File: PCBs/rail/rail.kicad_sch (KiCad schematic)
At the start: 3 parts

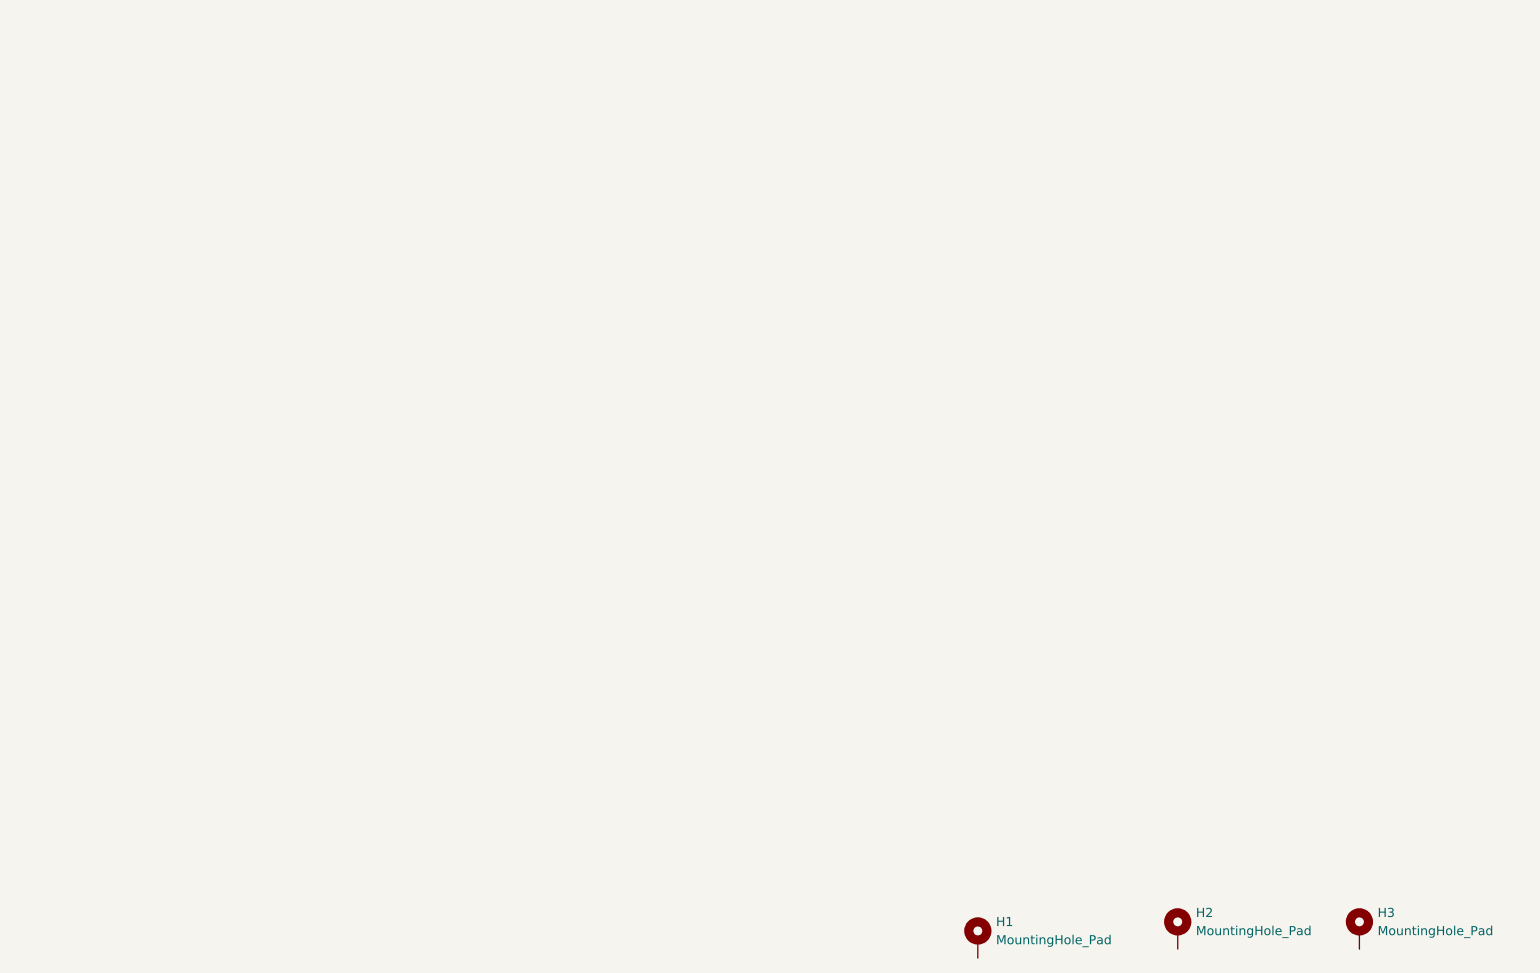
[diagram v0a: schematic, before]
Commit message: Torso, bogie and rail complete. Next up: revise hand and IMU board in conjunction
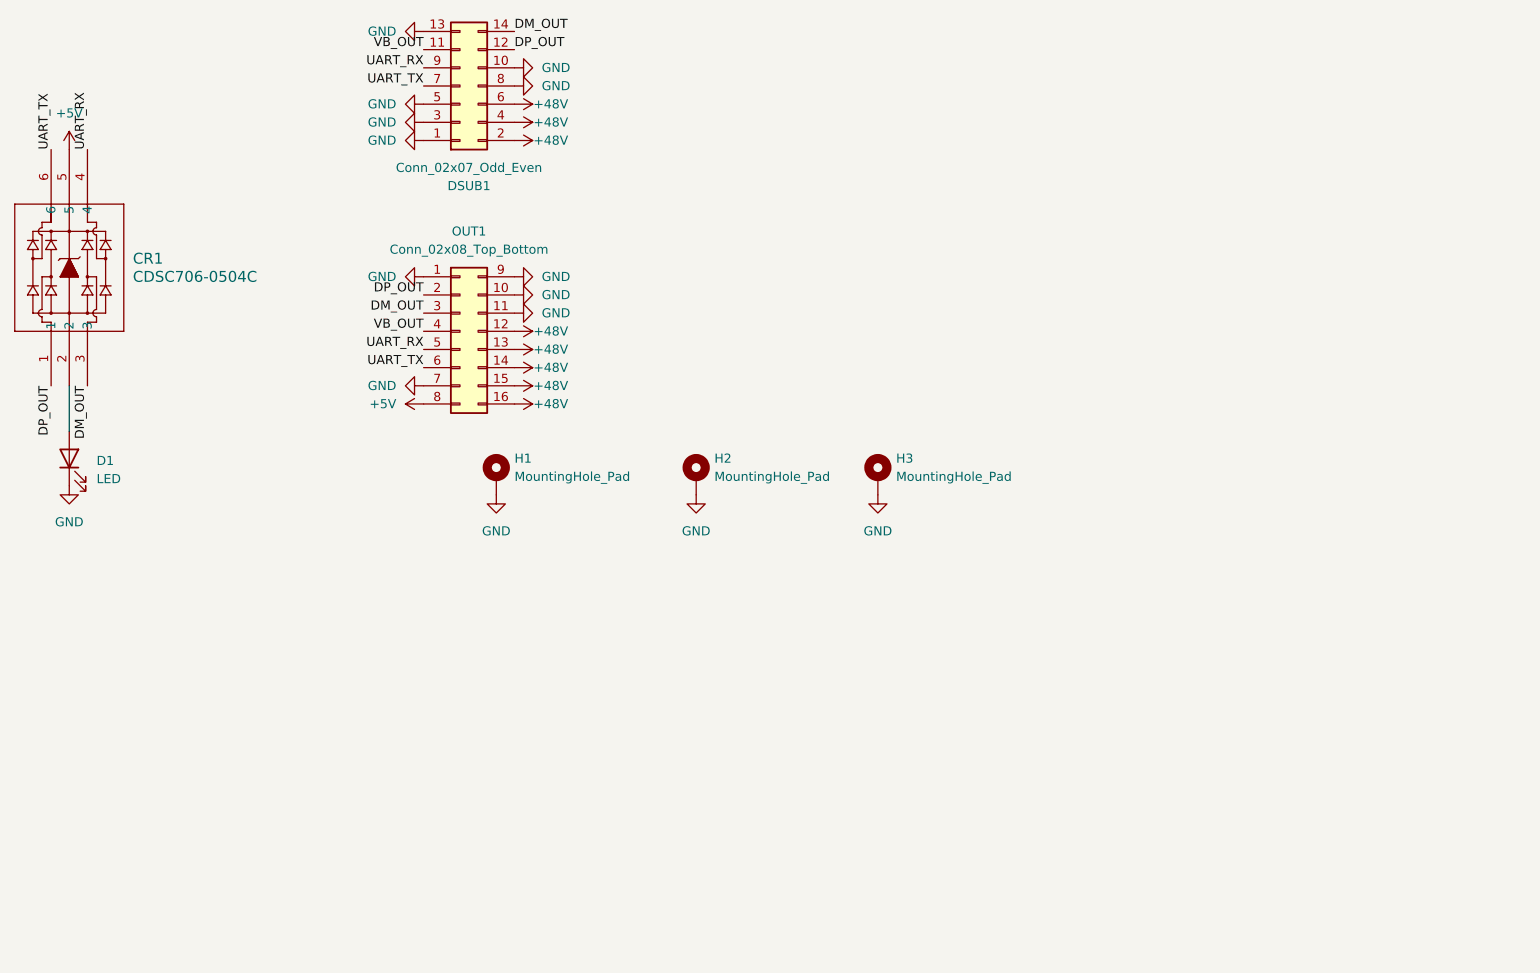
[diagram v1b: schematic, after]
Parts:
- added CR1: CDSC706-0504C, CDSC706-0504C_BRN, symbol CDSC706:CDSC706-0504C
- added D1: LED, LED_SMD:LED_0603_1608Metric, symbol Device:LED
- added DSUB1: Conn_02x07_Odd_Even, Connector_PinHeader_2.54mm:PinHeader_2x07_P2.54mm_Vertical, symbol Connector_Generic:Conn_02x07_Odd_Even
- added OUT1: Conn_02x08_Top_Bottom, 2-1761603-6:2-1761603-6_TYC, symbol Connector_Generic:Conn_02x08_Top_Bottom
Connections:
- net GND: now reaches H3.1
- net GND: now also H1.1, H2.1, D1.1 (K), DSUB1.1 (Pin_1), DSUB1.10 (Pin_10), DSUB1.13 (Pin_13), DSUB1.3 (Pin_3), DSUB1.5 (Pin_5), DSUB1.8 (Pin_8), OUT1.1 (Pin_1), OUT1.10 (Pin_10), OUT1.11 (Pin_11), OUT1.7 (Pin_7), OUT1.9 (Pin_9)
- new net: CR1.2, D1.2 (A)
- new net +48V: DSUB1.2 (Pin_2), DSUB1.4 (Pin_4), DSUB1.6 (Pin_6), OUT1.12 (Pin_12), OUT1.13 (Pin_13), OUT1.14 (Pin_14), OUT1.15 (Pin_15), OUT1.16 (Pin_16)
- new net +5V: CR1.5, OUT1.8 (Pin_8)
- new net DM_OUT: CR1.3, DSUB1.14 (Pin_14), OUT1.3 (Pin_3)
- new net DP_OUT: CR1.1, DSUB1.12 (Pin_12), OUT1.2 (Pin_2)
- new net UART_RX: CR1.4, DSUB1.9 (Pin_9), OUT1.5 (Pin_5)
- new net UART_TX: CR1.6, DSUB1.7 (Pin_7), OUT1.6 (Pin_6)
- new net VB_OUT: DSUB1.11 (Pin_11), OUT1.4 (Pin_4)
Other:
- moved on the sheet: H1, H2, H3

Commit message: merged changes from timertests, mostly documentation and such. Did not add tim6 config
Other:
- title: (none) -> Rail PCB
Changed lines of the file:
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@@
 (kicad_sch (version 20230121) (generator eeschema)
   (paper "A5")
+  (title_block
+    (title "Rail PCB")
+    (rev "Mk1.2")
+  )
   (wire (pts (xy 55.88 82.55) (xy 55.88 88.9))
     (stroke (width 0) (type default))
